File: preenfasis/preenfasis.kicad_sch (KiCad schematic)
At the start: 24 parts, among them J1 SMA H, J2 SMA H, J3 SMA H, J4 SMA H

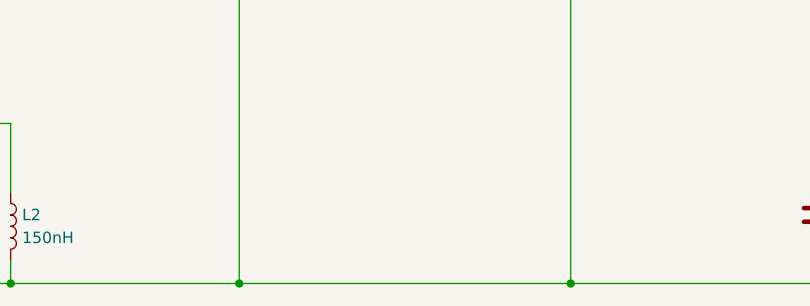
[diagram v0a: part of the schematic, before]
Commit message: Preenfasis v1.1
Se separaron los planos de tierra de ambas T
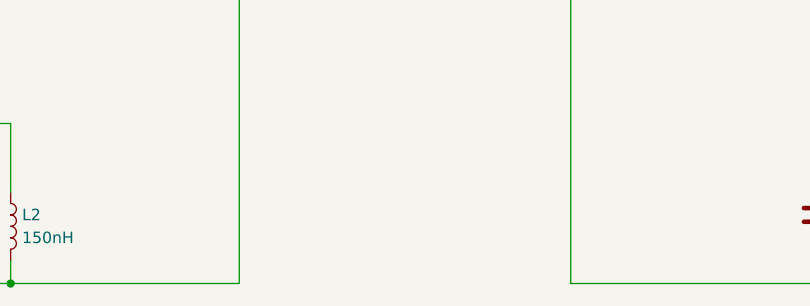
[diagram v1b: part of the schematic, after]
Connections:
- net at C2.1, J1.2 (Ext), J2.2 (Ext)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: no longer C4.1, J3.2 (Ext), J4.2 (Ext), L4.2
- new net: C4.1, J3.2 (Ext), J4.2 (Ext), L4.2
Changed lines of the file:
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@@
 		(title "Filtro de preenfasis")
 		(date "2025-01-06")
-		(rev "v1.0")
+		(rev "v1.1")
 		(company "Cotti Nicolas Gabriel")
 		(comment 1 "ncotti@frba.utn.edu.ar")
@@
 	(junction
 		(at 109.22 71.12)
-		(diameter 0)
-		(color 0 0 0 0)
-	)
-	(junction
-		(at 125.73 129.54)
 		(diameter 0)
 		(color 0 0 0 0)
@@
 	(junction
 		(at 212.09 71.12)
-		(diameter 0)
-		(color 0 0 0 0)
-	)
-	(junction
-		(at 162.56 129.54)
 		(diameter 0)
 		(color 0 0 0 0)
@@
 		)
 		(stroke
-			(width 0)
-			(type default)
-		)
-	)
-	(wire
-		(pts
-			(xy 125.73 129.54) (xy 162.56 129.54)
-		)
-		(stroke
